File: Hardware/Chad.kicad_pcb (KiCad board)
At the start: 4 copper layers, 30 x 60 mm, 130 parts, among them J1 RBUS, J2 GPIO Breakout, J3 ServoCH1, J4 ServoCH2, J5 USB_C_Receptacle_USB2.0, Q1 SSM3K15AMFV,L3F, U1 ESP32-S3, U2 SN65HVD230, U3 LM66200DRLR, U4 MAX77827AEFD+T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

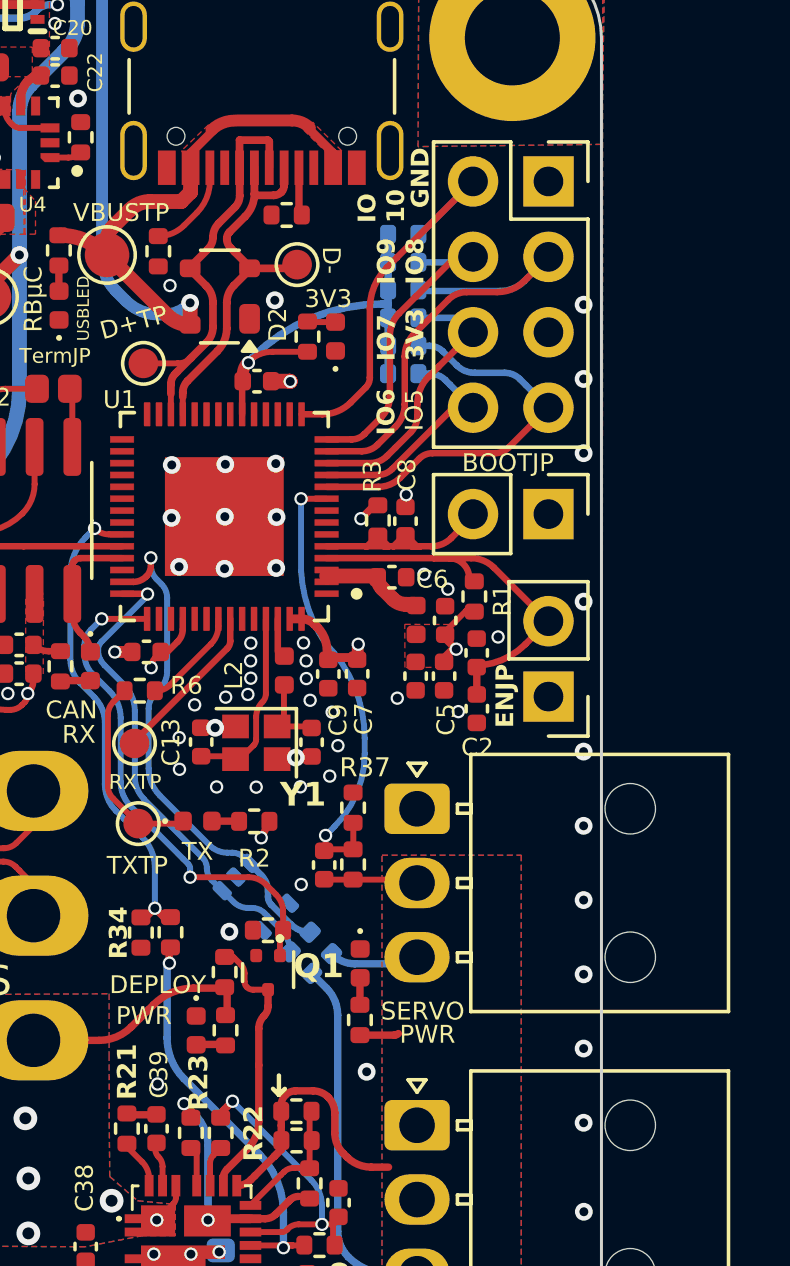
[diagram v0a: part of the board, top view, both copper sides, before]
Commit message: Added GPIO TVS protection
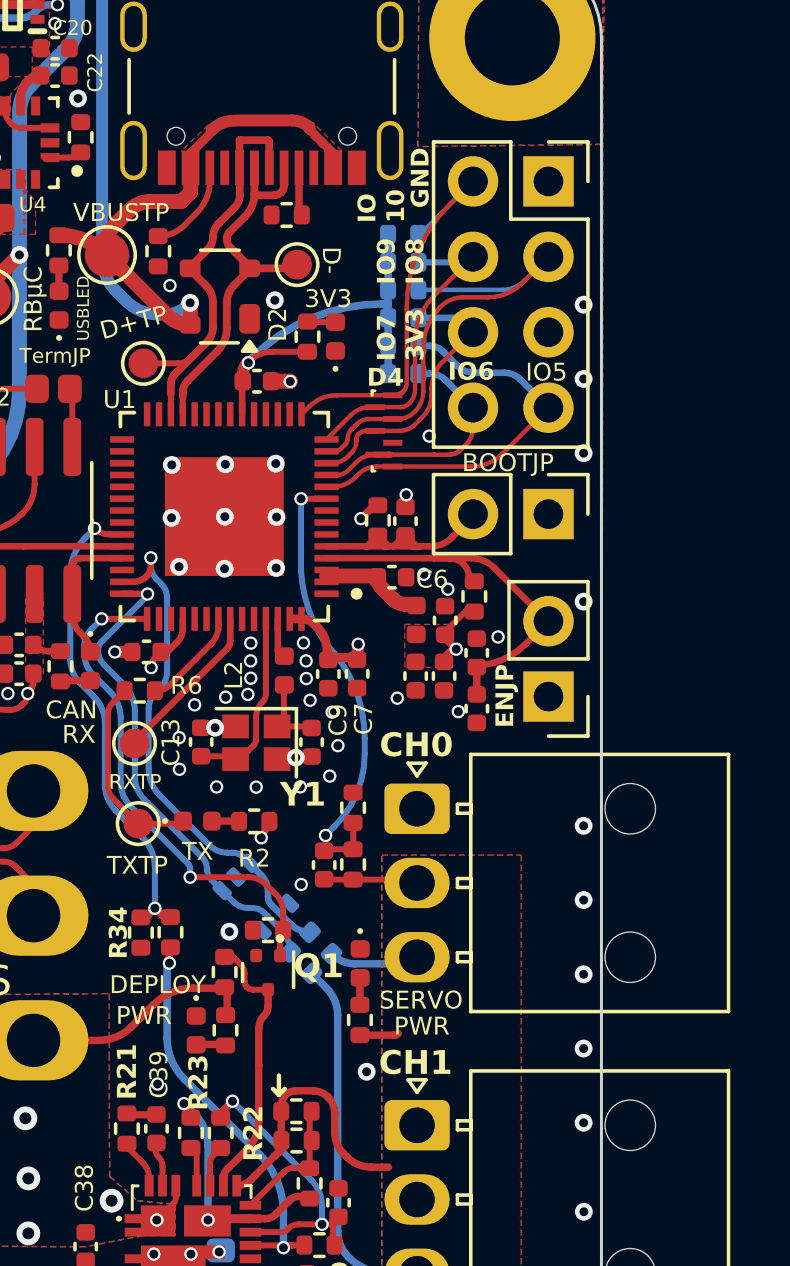
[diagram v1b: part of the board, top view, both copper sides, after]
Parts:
- added D4: RCLAMP3346PQTNT, iclr:RCLAMP3346PQTNT, F.Cu at (54.7, 58.3)
- C18: value TBD -> 160pF
- J3: value ServoCH1 -> ServoCH0
- J4: value ServoCH2 -> ServoCH1
- R42: value TBD -> 5.4R
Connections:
- D3 pad 1: /Servo2PWM -> /Servo1PWM
- D3 pad 3: /Servo1PWM -> /Servo0PWM
- R40 pad 1: /Servo1PWM -> /Servo0PWM
- R41 pad 1: /Servo2PWM -> /Servo1PWM
- U1 pad 41: /Servo1PWM -> /Servo0PWM
- U1 pad 42: /Servo2PWM -> /Servo1PWM
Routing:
- net /Servo0PWM: track 0.00 -> 17.2 mm, vias 0 -> 1
- net /Servo2PWM: track 16.6 -> 0.00 mm, vias 1 -> 0
- net /GPIO10: track 13.4 -> 14.5 mm
- net /GPIO6: track 8.12 -> 8.73 mm
- net /Servo1PWM: track 17.2 -> 16.6 mm
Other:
- board text added: "CH0"
- board text added: "CH1"

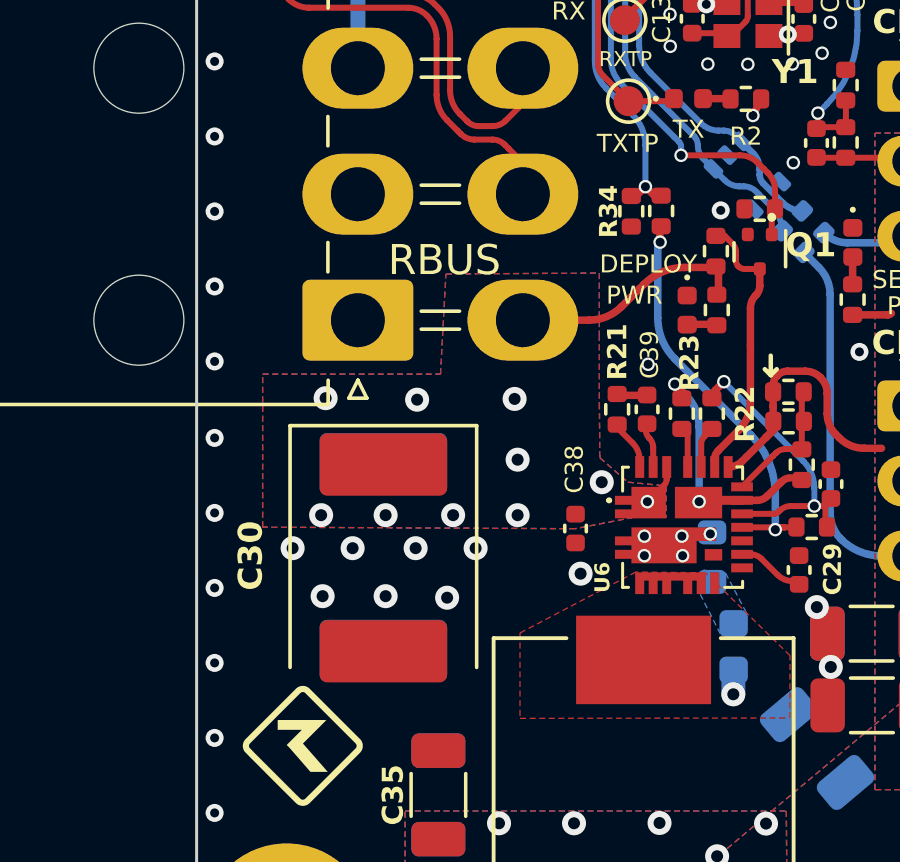
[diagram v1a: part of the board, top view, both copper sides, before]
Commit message: fixed pgood hardware issue
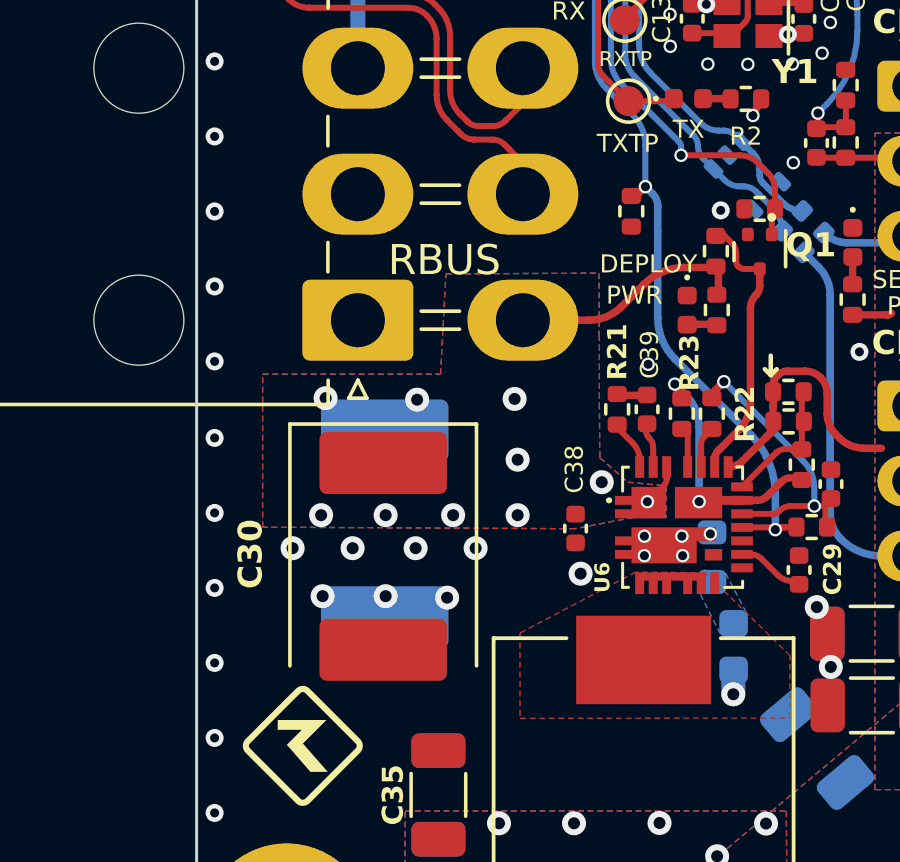
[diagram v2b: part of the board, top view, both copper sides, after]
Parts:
- removed R35: 1.5k, Resistor_SMD:R_0402_1005Metric
- R34: value 2.2k -> 18k
- R42: value 5.4R -> 5.1R
- moved LOGO1 1.88 mm to (47.7, 80.5)
- moved C32 1.12 mm to (38.3, 85.6)
- moved C30 0.05 mm to (38.2, 86.7)
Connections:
- R18 pad 2: /buckC/PGOOD -> /BuckPGOOD
- U6 pad 14: /buckC/PGOOD -> /BuckPGOOD
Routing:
- net /BuckPGOOD: track 16.2 -> 30.8 mm, vias 2 -> 3
- net /buckC/PGOOD: track 13.8 -> 0.00 mm, vias 2 -> 0
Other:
- board text removed: "Batch Number - JLCJLCJLCJLC"
